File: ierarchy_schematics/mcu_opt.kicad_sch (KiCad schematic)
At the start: 5 parts, among them U2 MCP1790-3302E/DB, U7 AM6TW-2412SZ

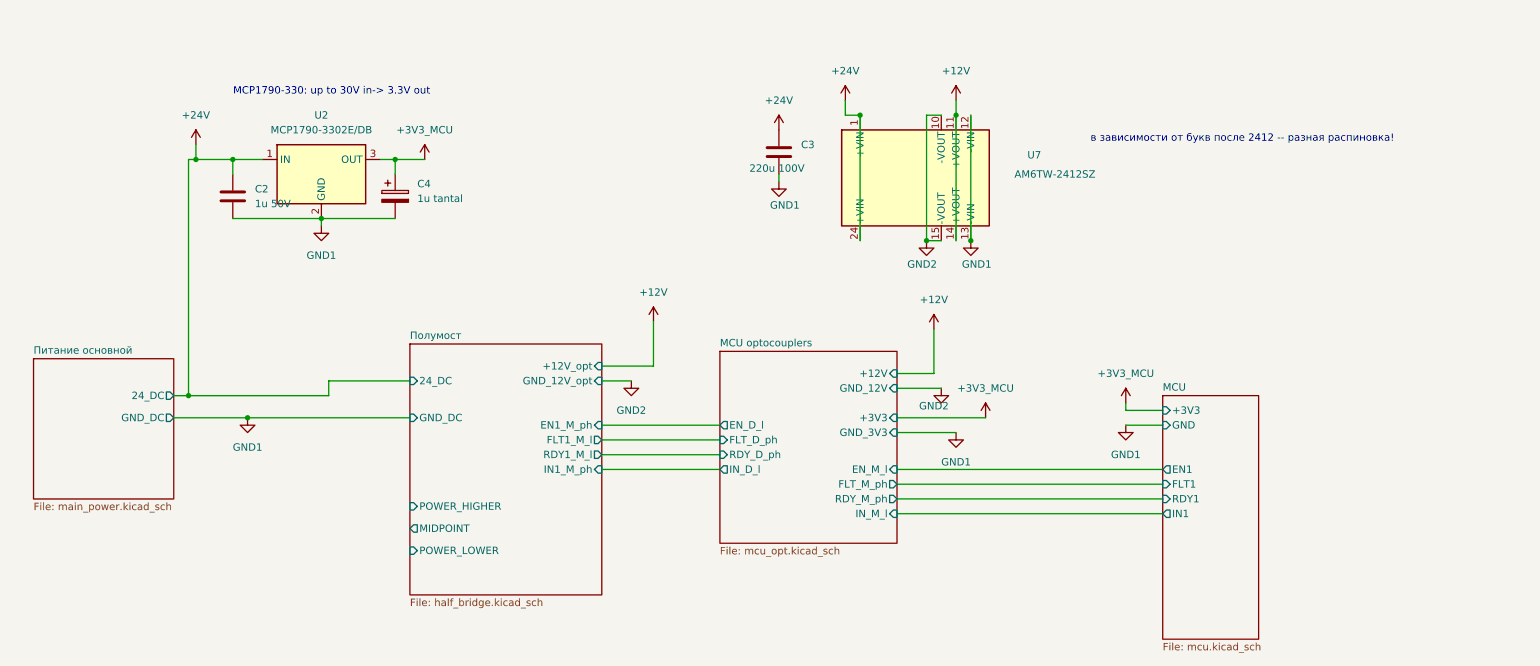
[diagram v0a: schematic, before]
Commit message: Half bridge + power + MCU + optocouplers for one driver.
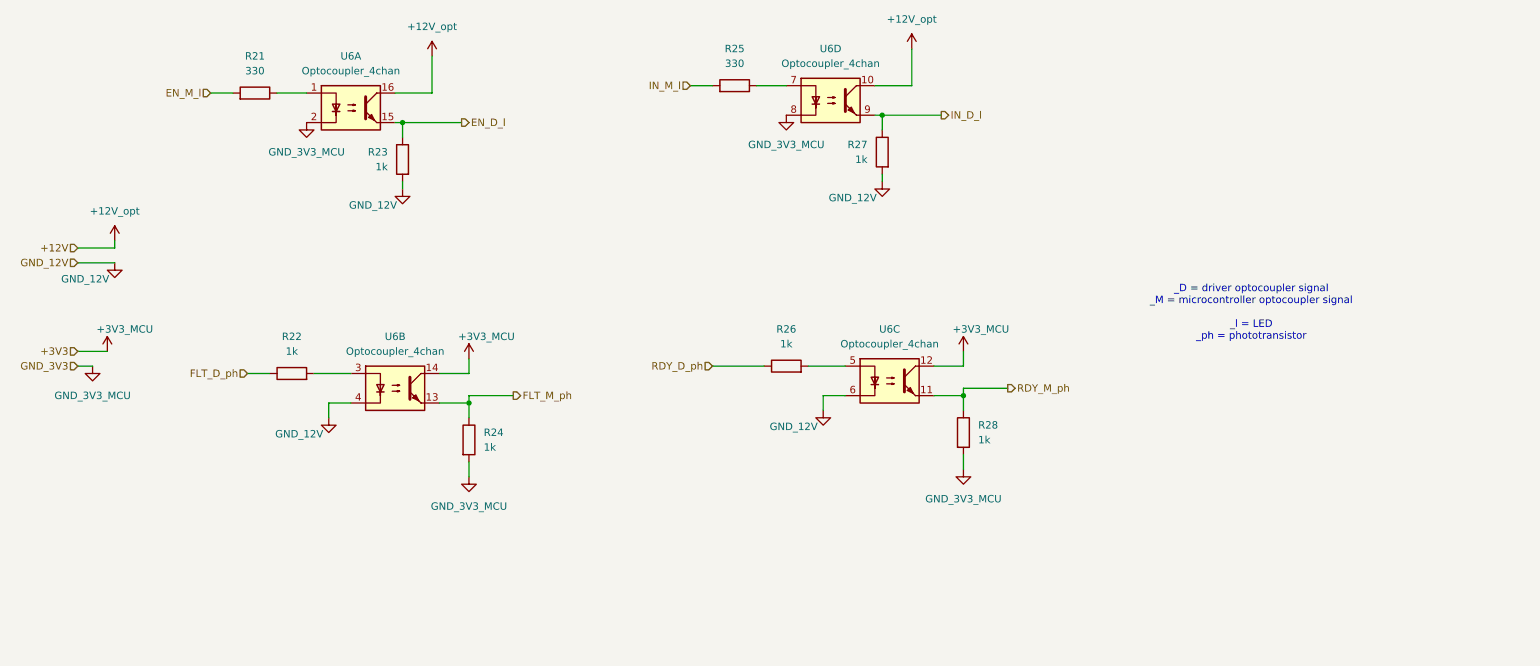
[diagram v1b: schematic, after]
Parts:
- removed C2: 1u 50V, Capacitor_SMD:C_0603_1608Metric_Pad1.08x0.95mm_HandSolder, symbol Device:C
- removed C3: 220u 100V, symbol Device:C
- removed C4: 1u tantal, Capacitor_Tantalum_SMD:CP_EIA-3216-10_Kemet-I_HandSolder, symbol Device:C_Polarized
- removed U2: MCP1790-3302E/DB, Package_TO_SOT_SMD:SOT-223-3_TabPin2, symbol Regulator_Linear:LT1963AxST-1.5
- removed U7: AM6TW-2412SZ, Package_DIP:DIP-24_18.0mmx34.29mm_W15.24mm_LongPads, symbol Regulator_Linear:LDK130-ADJ_DFN6
- added R21, R25: 330, Resistor_SMD:R_0805_2012Metric_Pad1.20x1.40mm_HandSolder, symbol Device:R
- added R22, R26: 1k, Resistor_SMD:R_0805_2012Metric_Pad1.20x1.40mm_HandSolder, symbol Device:R
- added R23, R24, R27, R28: 1k, Resistor_SMD:R_0402_1005Metric_Pad0.72x0.64mm_HandSolder, symbol Device:R
- added U6: Optocoupler_4chan, Package_SO:SOIC-16W_7.5x10.3mm_P1.27mm, symbol Tamara:Optocoupler_4chan
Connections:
- net +3V3_MCU: now also U6.12, U6.14
- new net: R25.1, U6.7
- new net: R26.2, U6.5
- new net: R22.2, U6.3
- new net: R21.1, U6.1
- new net +12V_opt: U6.10, U6.16
- new net EN_D_l: R23.1, U6.15
- new net EN_M_l: R21.2
- new net FLT_D_ph: R22.1
- new net FLT_M_ph: R24.1, U6.13
- new net GND_12V: R23.2, R27.2, U6.4, U6.6
- new net GND_3V3_MCU: R24.2, R28.2, U6.2, U6.8
- new net IN_D_l: R27.1, U6.9
- new net IN_M_l: R25.2
- new net RDY_D_ph: R26.1
- new net RDY_M_ph: R28.1, U6.11
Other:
- removed sheet MCU
- removed sheet MCU optocouplers
- removed sheet Питание основной
- removed sheet Полумост
- note added: "_D = driver optocoupler signal _M = microcontroller optocoupler signal _l = LED _ph = phototransistor"
- note removed: "MCP1790-330: up to 30V in-> 3.3V out"
- note removed: "в зависимости от букв после 2412 -- разная распиновка!"
